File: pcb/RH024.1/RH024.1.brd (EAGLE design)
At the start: 49.5 x 49.5 mm, 29 parts, among them CN1 USB, CN4 FTDI, U2 FT232RLSSOP, U3 REG1117

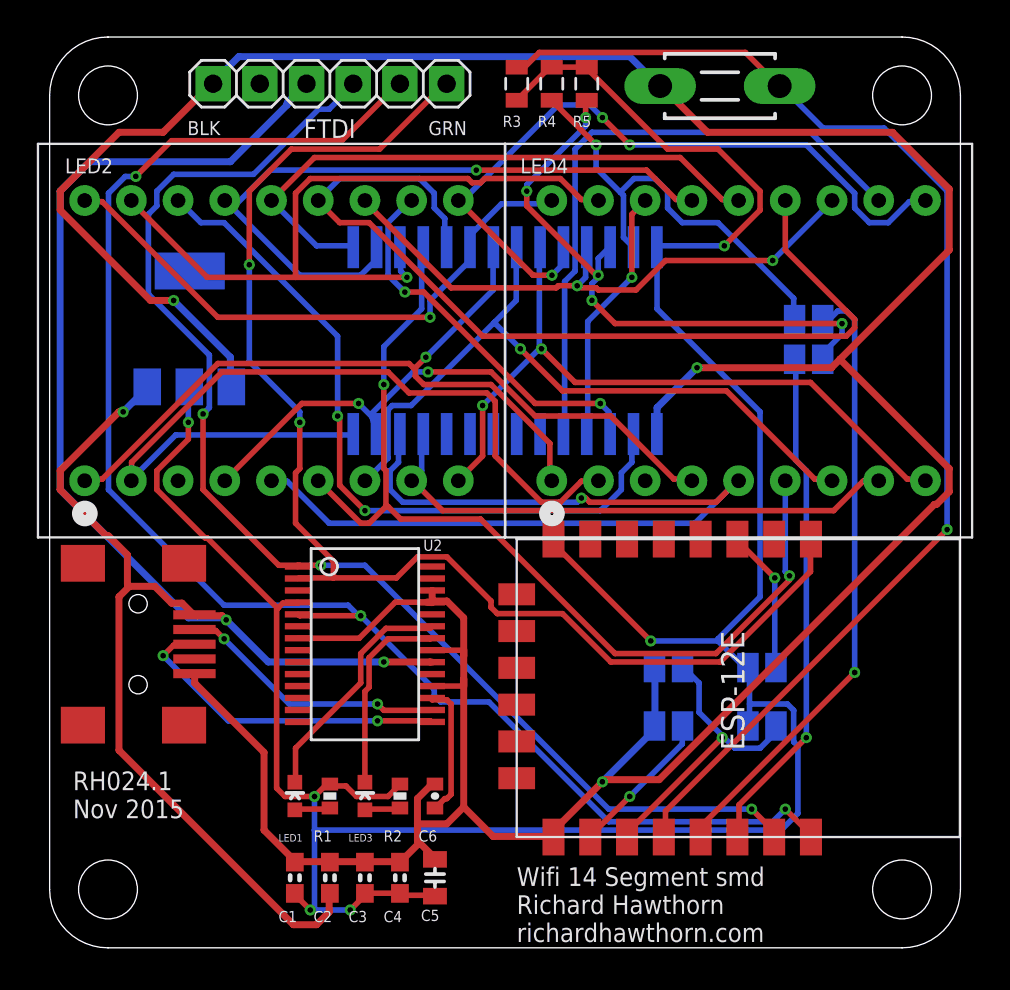
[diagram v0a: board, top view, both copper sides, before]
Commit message: update position of usb connector
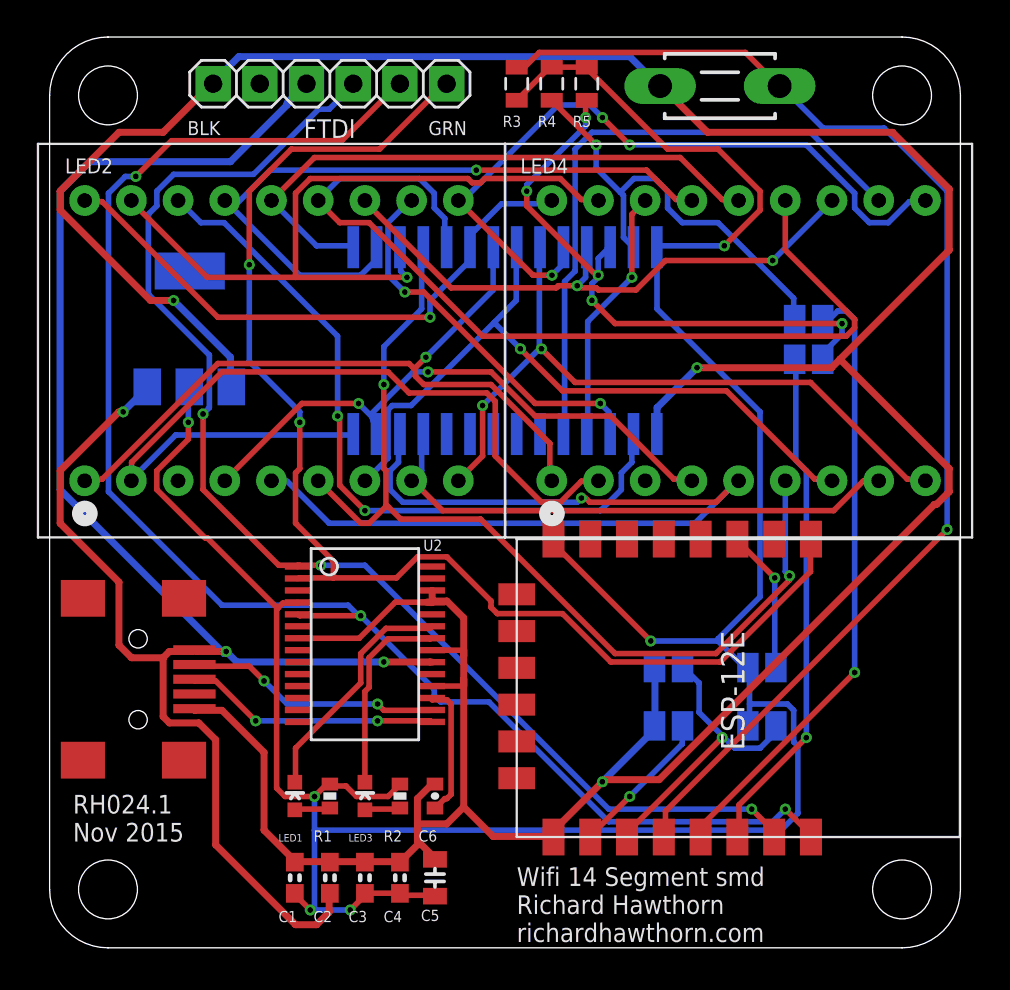
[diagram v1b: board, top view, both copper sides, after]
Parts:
- moved CN1 1.91 mm to (3.81, 14.6)
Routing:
- net D+: track 18.1 -> 13.9 mm
- net GND: track 199.1 -> 198.1 mm
- net PWR: track 102.6 -> 101.7 mm
- net D-: track 14.8 -> 14.0 mm
